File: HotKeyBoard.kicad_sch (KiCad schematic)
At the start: 414 parts, among them J1 Conn_01x04_Pin, J2 Conn_01x04_Pin, J3 USB_VOLTAGE Measuring Point, J4 LED_VOLTAGE Measuring Point 1, J5 LED_VOLTAGE Measuring Point 2, Q1 IRLZ34N, Q2 IRLZ34N, Q3 IRLZ34N, Q4 IRLZ34N, Q5 IRLZ34N, Q6 IRLZ34N, SW1 SW_Push, SW10 SW_Push, SW11 SW_Push, SW12 SW_Push, SW13 SW_Push, SW14 SW_Push, SW15 SW_Push, SW16 SW_Push, SW17 SW_Push, SW18 SW_Push, SW19 SW_Push, SW2 SW_Push, SW20 SW_Push, SW21 SW_Push, SW22 SW_Push, SW23 SW_Push, SW24 SW_Push, SW25 SW_Push, SW26 SW_Push, SW27 SW_Push, SW28 SW_Push, SW29 SW_Push, SW3 SW_Push, SW30 SW_Push, SW31 SW_Push, SW32 SW_Push, SW33 SW_Push, SW34 SW_Push, SW35 SW_Push, SW36 SW_Push, SW37 SW_Push, SW38 SW_Push, SW39 SW_Push, SW4 SW_Push, SW40 SW_Push, SW41 SW_Push, SW42 SW_Push, SW43 SW_Push, SW44 SW_Push, SW45 SW_Push, SW46 SW_Push, SW47 SW_Push, SW48 SW_Push, SW49 SW_Push, SW5 SW_Push, SW50 SW_Push, SW51 SW_Push, SW52 SW_Push, SW53 SW_Push, SW54 SW_Push, SW55 SW_Push, SW56 SW_Push, SW57 SW_Push, SW58 SW_Push, SW59 SW_Push, SW6 SW_Push, SW60 SW_Push, SW61 SW_Push, SW62 SW_Push, SW63 SW_Push, SW64 SW_Push, SW65 SW_Push, SW66 SW_Push, SW67 SW_Push, SW68 SW_Push, SW69 SW_Push, SW7 SW_Push, SW70 SW_Push, SW71 SW_Push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

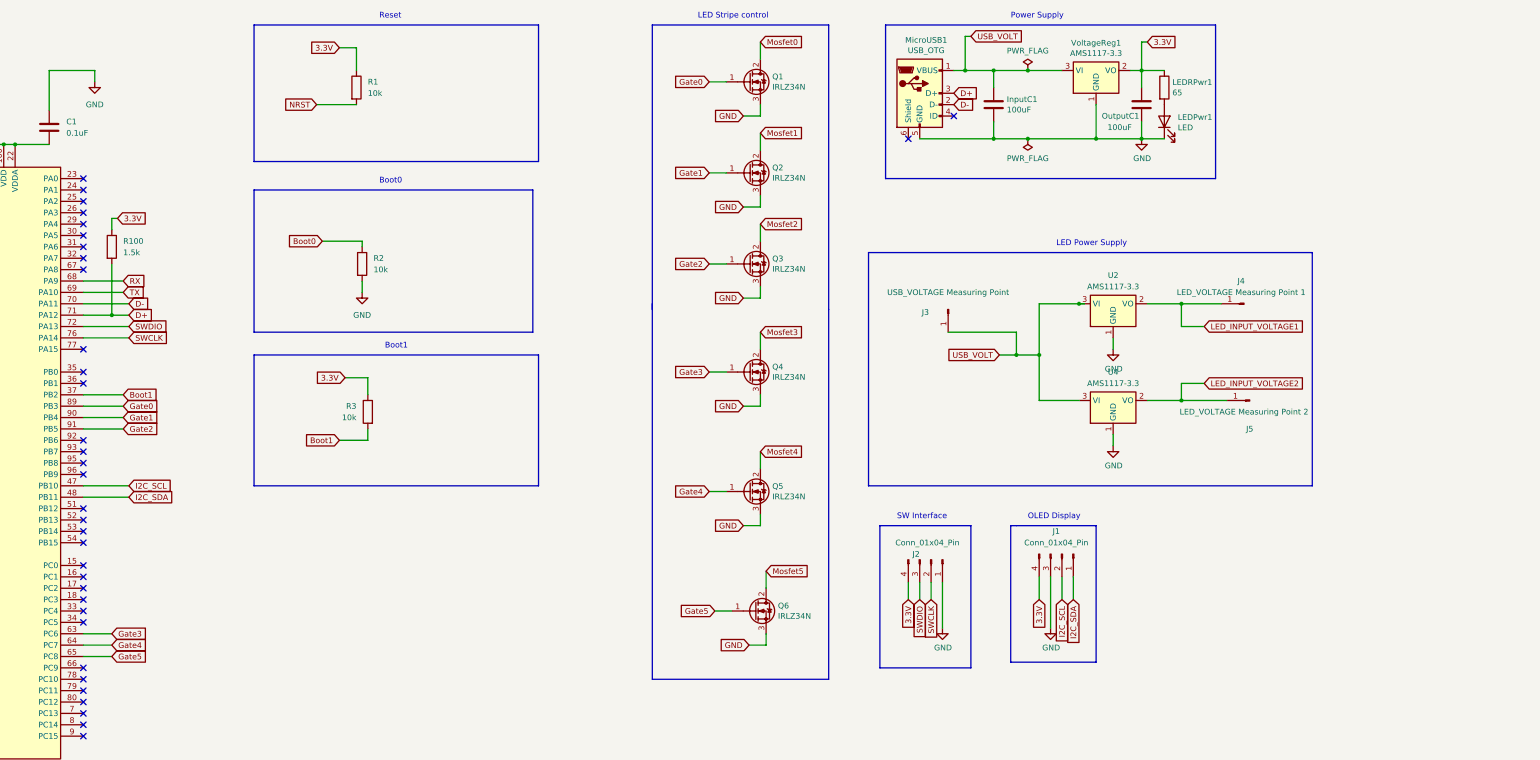
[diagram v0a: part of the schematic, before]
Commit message: Added overbridging of mosfets
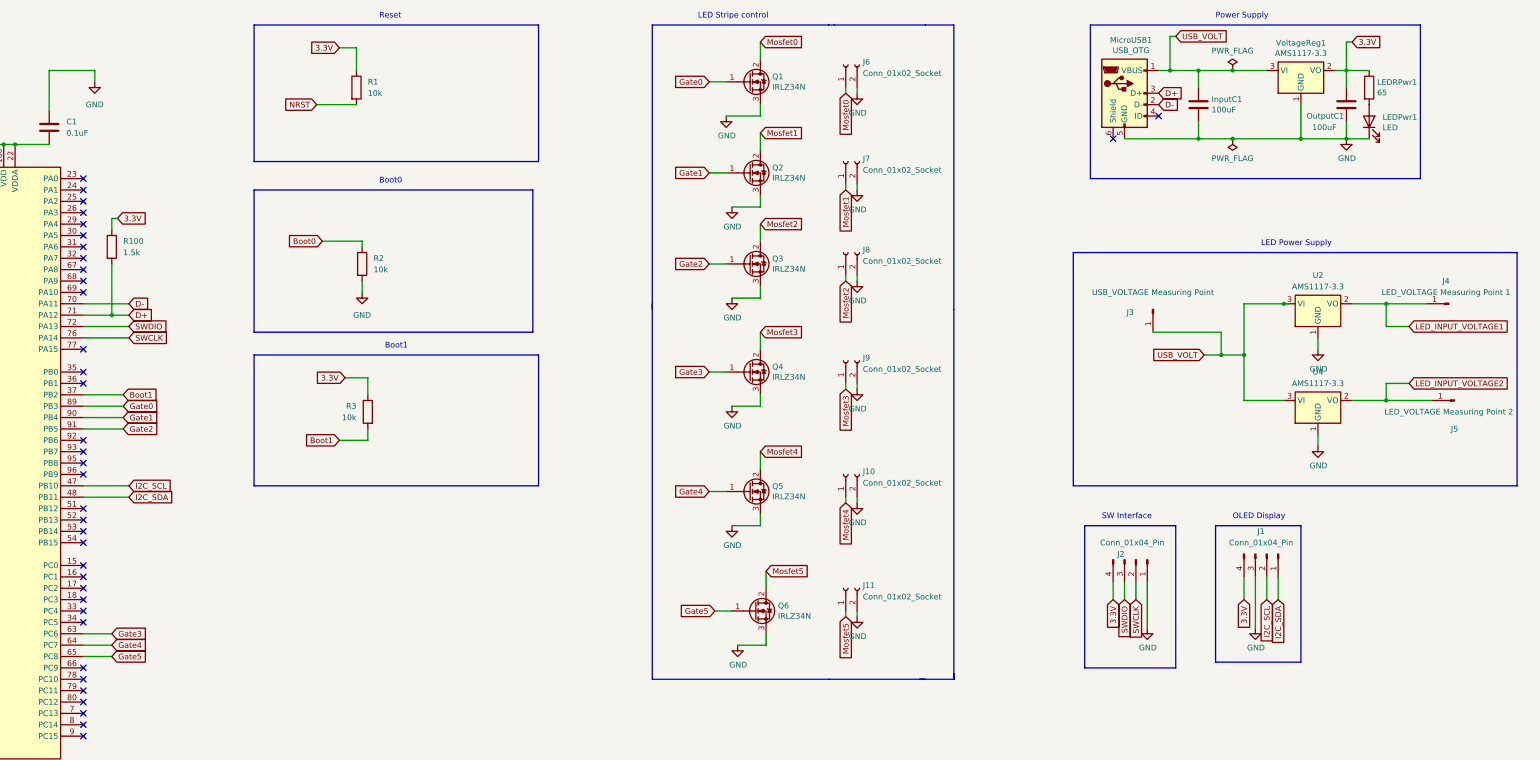
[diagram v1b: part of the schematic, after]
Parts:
- added J10, J11, J6, J7, J8, J9: Conn_01x02_Socket, Connector_PinHeader_2.54mm:PinHeader_1x02_P2.54mm_Vertical, symbol Connector:Conn_01x02_Socket
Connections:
- net GND: now also J10.2 (Pin_2), J11.2 (Pin_2), J6.2 (Pin_2), J7.2 (Pin_2), J8.2 (Pin_2), J9.2 (Pin_2)
- net Mosfet0: now also J6.1 (Pin_1)
- net Mosfet1: now also J7.1 (Pin_1)
- net Mosfet2: now also J8.1 (Pin_1)
- net Mosfet3: now also J9.1 (Pin_1)
- net Mosfet4: now also J10.1 (Pin_1)
- net Mosfet5: now also J11.1 (Pin_1)
- net RX: no longer names the net of U1.68 (PA9)
- net TX: no longer names the net of U1.69 (PA10)
- no-connect marks 37 -> 39
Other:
- moved on the sheet: InputC1, J1, J2, J3, J4, J5, LEDPwr1, LEDRPwr1, MicroUSB1, OutputC1, U2, U4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

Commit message: Added THT micro usb
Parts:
- MicroUSB1: footprint Connector_USB:USB_Micro-B_Molex_47346-0001 -> Connector_USB:USB_Micro-B_Amphenol_10118194_Horizontal; LCSC (none) -> C114094
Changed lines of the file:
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@@
       (effects (font (size 1.27 1.27)))
     )
-    (property "Footprint" "Connector_USB:USB_Micro-B_Molex_47346-0001" (at 499.11 36.83 0)
+    (property "Footprint" "Connector_USB:USB_Micro-B_Amphenol_10118194_Horizontal" (at 499.11 36.83 0)
       (effects (font (size 1.27 1.27)) hide)
     )
@@
       (effects (font (size 1.27 1.27)) hide)
     )
+    (property "LCSC" "C114094" (at 495.3 35.56 0)
+      (effects (font (size 1.27 1.27)) hide)
+    )

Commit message: Changed micro usb port
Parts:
- MicroUSB1: footprint Connector_USB:USB_Micro-B_Amphenol_10118194_Horizontal -> Library:MICRO-USB_SMD_USB-MR-D-034; LCSC C114094 -> C2927005
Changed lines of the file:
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@@
       (effects (font (size 1.27 1.27)))
     )
-    (property "Footprint" "Connector_USB:USB_Micro-B_Amphenol_10118194_Horizontal" (at 499.11 36.83 0)
+    (property "Footprint" "Library:MICRO-USB_SMD_USB-MR-D-034" (at 499.11 36.83 0)
       (effects (font (size 1.27 1.27)) hide)
     )
@@
       (effects (font (size 1.27 1.27)) hide)
     )
-    (property "LCSC" "C114094" (at 495.3 35.56 0)
+    (property "LCSC" "C2927005" (at 495.3 35.56 0)
       (effects (font (size 1.27 1.27)) hide)
     )

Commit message: Switched micro usb again
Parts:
- MicroUSB1: footprint Library:MICRO-USB_SMD_USB-MR-D-034 -> Library:MICRO-USB-SMD_5P-P0.65-H-F_U254-051T-4BH81-S2S; LCSC C2927005 -> C381144
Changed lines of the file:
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@@
       (effects (font (size 1.27 1.27)))
     )
-    (property "Footprint" "Library:MICRO-USB_SMD_USB-MR-D-034" (at 499.11 36.83 0)
+    (property "Footprint" "Library:MICRO-USB-SMD_5P-P0.65-H-F_U254-051T-4BH81-S2S" (at 499.11 36.83 0)
       (effects (font (size 1.27 1.27)) hide)
     )
@@
       (effects (font (size 1.27 1.27)) hide)
     )
-    (property "LCSC" "C2927005" (at 495.3 35.56 0)
+    (property "LCSC" "C381144" (at 495.3 35.56 0)
       (effects (font (size 1.27 1.27)) hide)
     )

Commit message: Finished schematic
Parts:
- removed C1: 0.1uF, Capacitor_SMD:C_0402_1005Metric, symbol Device:C
- removed C2: 1uF, Capacitor_SMD:C_0603_1608Metric, symbol Device:C
- removed InputC1, OutputC1: 100uF, Capacitor_SMD:C_1206_3216Metric, symbol Device:C
- removed J10, J11, J7, J8, J9: Conn_01x02_Socket, Connector_PinHeader_2.54mm:PinHeader_1x02_P2.54mm_Vertical, symbol Connector:Conn_01x02_Socket
- removed J2: Conn_01x04_Pin, Connector_PinHeader_2.54mm:PinHeader_1x04_P2.54mm_Vertical, symbol Connector:Conn_01x04_Pin
- removed J3: USB_VOLTAGE Measuring Point, Connector_PinHeader_2.54mm:PinHeader_1x01_P2.54mm_Vertical, symbol Connector:Conn_01x01_Pin
- removed J4: LED_VOLTAGE Measuring Point 1, Connector_PinHeader_2.54mm:PinHeader_1x01_P2.54mm_Vertical, symbol Connector:Conn_01x01_Pin
- removed J5: LED_VOLTAGE Measuring Point 2, Connector_PinHeader_2.54mm:PinHeader_1x01_P2.54mm_Vertical, symbol Connector:Conn_01x01_Pin
- removed LEDPwr1: LED, LED_SMD:LED_0402_1005Metric, symbol Device:LED
- removed LEDRPwr1: 65, Resistor_SMD:R_0603_1608Metric, symbol Device:R
- removed MicroUSB1: USB_OTG, Library:MICRO-USB-SMD_5P-P0.65-H-F_U254-051T-4BH81-S2S, symbol Connector:USB_OTG
- removed Q2, Q3, Q4, Q5, Q6: IRLZ34N, Package_TO_SOT_SMD:TO-263-2, symbol Transistor_FET:IRLZ34N
- removed R1, R2, R3: 10k, Resistor_SMD:R_0603_1608Metric, symbol Device:R
- removed R100: 1.5k, Resistor_SMD:R_0603_1608Metric, symbol Device:R
- removed U1: STM32F103VBTx, Package_QFP:LQFP-100_14x14mm_P0.5mm, symbol MCU_ST_STM32F1:STM32F103VBTx
- removed U2, U4, VoltageReg1: AMS1117-3.3, Package_TO_SOT_SMD:SOT-223-3_TabPin2, symbol Regulator_Linear:AMS1117-3.3
- added J2, J3: Conn_01x20_Pin, Connector_PinHeader_2.54mm:PinHeader_1x20_P2.54mm_Vertical, symbol Connector:Conn_01x20_Pin
- R10, R11, R12, R13, R14, R15, R16, R17, R18, R19, R20, R21, R22, R23, R24, R25, R26, R27, R28, R29, R30, R31, R32, R33, R34, R35, R36, R37, R38, R39, R4, R40, R42, R43, R44, R45, R46, R47, R48, R49, R5, R50, R51, R52, R53, R54, R55, R56, R57, R58, R59, R6, R60, R61, R62, R63, R64, R65, R66, R67, R68, R69, R7, R70, R71, R72, R73, R74, R75, R76, R77, R78, R79, R8, R80, R81, R82, R83, R84, R85, R86, R87, R88, R89, R9, R90, R91, R92, R93, R94, R95, R96, R97, R98, R99: LCSC C307279 -> C881395
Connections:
- net LED_INPUT_VOLTAGE2 is gone; now on net 5V: R52.1, R53.1, R54.1, R55.1, R56.1, R57.1, R58.1, R59.1, R60.1, R61.1, R62.1, R63.1, R64.1, R65.1, R66.1, R67.1, R68.1, R69.1, R70.1, R71.1, R72.1, R73.1, R74.1, R75.1, R76.1, R77.1, R78.1, R79.1, R80.1, R81.1, R82.1, R83.1, R84.1, R85.1, R86.1, R87.1, R88.1, R89.1, R90.1, R91.1, R92.1, R93.1, R94.1, R95.1, R96.1, R97.1, R98.1, R99.1
- net Mosfet1 is gone; now on net Mosfet0: D113.1 (K), D114.1 (K), D115.1 (K), D116.1 (K), D117.1 (K), D118.1 (K), D119.1 (K), D120.1 (K), D121.1 (K), D122.1 (K), D123.1 (K), D124.1 (K), D125.1 (K), D126.1 (K), D127.1 (K), D128.1 (K)
- net Mosfet2 is gone; now on net Mosfet0: D129.1 (K), D130.1 (K), D131.1 (K), D132.1 (K), D133.1 (K), D134.1 (K), D135.1 (K), D136.1 (K), D137.1 (K), D138.1 (K), D139.1 (K), D140.1 (K), D141.1 (K), D142.1 (K), D143.1 (K), D144.1 (K)
- net Mosfet3 is gone; now on net Mosfet0: D145.1 (K), D146.1 (K), D147.1 (K), D148.1 (K), D149.1 (K), D150.1 (K), D151.1 (K), D152.1 (K), D153.1 (K), D154.1 (K), D155.1 (K), D156.1 (K), D157.1 (K), D158.1 (K), D159.1 (K), D160.1 (K)
- net Mosfet4 is gone; now on net Mosfet0: D161.1 (K), D162.1 (K), D163.1 (K), D164.1 (K), D165.1 (K), D166.1 (K), D167.1 (K), D168.1 (K), D169.1 (K), D170.1 (K), D171.1 (K), D172.1 (K), D173.1 (K), D174.1 (K), D175.1 (K), D176.1 (K)
- net Mosfet5 is gone; now on net Mosfet0: D177.1 (K), D178.1 (K), D179.1 (K), D180.1 (K), D181.1 (K), D182.1 (K), D183.1 (K), D184.1 (K), D185.1 (K), D186.1 (K), D187.1 (K), D188.1 (K), D189.1 (K), D190.1 (K), D191.1 (K), D192.1 (K)
- net 3.3V: now also J2.20 (Pin_20), J3.3 (Pin_3)
- net Col0: now also J3.8 (Pin_8)
- net Col1: now also J3.7 (Pin_7)
- net Col10: now also J2.1 (Pin_1)
- net Col11: now also J2.2 (Pin_2)
- net Col12: now also J2.3 (Pin_3)
- net Col13: now also J2.4 (Pin_4)
- net Col14: now also J2.5 (Pin_5)
- net Col2: now also J3.9 (Pin_9)
- net Col3: now also J2.13 (Pin_13)
- net Col4: now also J2.14 (Pin_14)
- net Col5: now also J2.15 (Pin_15)
- net Col6: now also J2.16 (Pin_16)
- net Col7: now also J2.17 (Pin_17)
- net Col8: now also J3.6 (Pin_6)
- net Col9: now also J3.5 (Pin_5)
- net GND: now also J2.19 (Pin_19), J3.1 (Pin_1), J3.2 (Pin_2)
- net Row0: now also J3.16 (Pin_16)
- net Row1: now also J3.15 (Pin_15)
- net Row2: now also J3.14 (Pin_14)
- net Row3: now also J3.13 (Pin_13)
- net Row4: now also J3.12 (Pin_12)
- net Row5: now also J3.11 (Pin_11)
- net Gate0 renamed LEDControl
- net LEDControl: now also J2.6 (Pin_6)
- net LED_INPUT_VOLTAGE1 renamed 5V
- net 5V: now also J2.18 (Pin_18)
- new net A10: J2.7 (Pin_7)
- new net A11: J2.8 (Pin_8)
- new net A12: J2.9 (Pin_9)
- new net A15: J2.10 (Pin_10)
- new net A6: J3.10 (Pin_10)
- new net B3: J2.11 (Pin_11)
- new net B4: J2.12 (Pin_12)
- new net C13: J3.19 (Pin_19)
- new net C14: J3.18 (Pin_18)
- new net C15: J3.17 (Pin_17)
- new net Reset: J3.4 (Pin_4)
- new net VB: J3.20 (Pin_20)
- no-connect marks 39 -> 0
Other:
- note removed: "Boot0"
- note removed: "Boot1"
- note removed: "LED Power Supply"
- note removed: "Power Supply"
- note removed: "Reset"
- note removed: "SW Interface"
- moved on the sheet: D1, D10, D100, D101, D102, D103, D104, D105, D106, D107, D108, D109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

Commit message: Finished layout
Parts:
- Q1: footprint Package_TO_SOT_SMD:TO-263-2 -> Package_TO_SOT_THT:TO-220-3_Vertical
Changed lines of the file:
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@@
       (effects (font (size 1.27 1.27)) (justify left))
     )
-    (property "Footprint" "Package_TO_SOT_SMD:TO-263-2" (at 411.48 224.155 0)
+    (property "Footprint" "Package_TO_SOT_THT:TO-220-3_Vertical" (at 411.48 224.155 0)
       (effects (font (size 1.27 1.27) italic) (justify left) hide)
     )

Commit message: Fixed resistor
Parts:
- R41: LCSC C307279 -> C881395
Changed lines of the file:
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@@
       (effects (font (size 1.27 1.27)) hide)
     )
-    (property "LCSC" "C307279" (at 139.7 246.38 0)
+    (property "LCSC" "C881395" (at 139.7 246.38 0)
       (effects (font (size 1.27 1.27)) hide)
     )

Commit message: Added multiple mosfets
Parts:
- added J4, J5: Conn_01x02_Socket, Connector_PinHeader_2.54mm:PinHeader_1x02_P2.54mm_Vertical, symbol Connector:Conn_01x02_Socket
- added Q2, Q3: IRLZ34N, Package_TO_SOT_THT:TO-220-3_Vertical, symbol Transistor_FET:IRLZ34N
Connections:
- net GND: now also J4.2 (Pin_2), J5.2 (Pin_2), Q2.3 (S), Q3.3 (S)
- net Mosfet0: no longer D113.1 (K), D114.1 (K), D115.1 (K), D116.1 (K), D117.1 (K), D118.1 (K), D119.1 (K), D120.1 (K), D121.1 (K), D122.1 (K), D123.1 (K), D124.1 (K), D125.1 (K), D126.1 (K), D127.1 (K), D128.1 (K), D129.1 (K), D130.1 (K), D131.1 (K), D132.1 (K), D133.1 (K), D134.1 (K), D135.1 (K), D136.1 (K), D137.1 (K), D138.1 (K), D139.1 (K), D140.1 (K), D141.1 (K), D142.1 (K), D143.1 (K), D144.1 (K), D145.1 (K), D146.1 (K), D147.1 (K), D148.1 (K), D149.1 (K), D150.1 (K), D151.1 (K), D152.1 (K), D153.1 (K), D154.1 (K), D155.1 (K), D156.1 (K), D157.1 (K), D158.1 (K), D159.1 (K), D160.1 (K), D161.1 (K), D162.1 (K), D163.1 (K), D164.1 (K), D165.1 (K), D166.1 (K), D167.1 (K), D168.1 (K), D169.1 (K), D170.1 (K), D171.1 (K), D172.1 (K), D173.1 (K), D174.1 (K), D175.1 (K), D176.1 (K), D177.1 (K), D178.1 (K), D179.1 (K), D180.1 (K), D181.1 (K), D182.1 (K), D183.1 (K), D184.1 (K), D185.1 (K), D186.1 (K), D187.1 (K), D188.1 (K), D189.1 (K), D190.1 (K), D191.1 (K), D192.1 (K)
- net A10 renamed LEDControl1
- net LEDControl1: now also Q2.1 (G)
- net A6 renamed LEDControl2
- net LEDControl2: now also Q3.1 (G)
- net LEDControl renamed LEDControl0
- new net Mosfet1: D113.1 (K), D114.1 (K), D115.1 (K), D116.1 (K), D117.1 (K), D118.1 (K), D119.1 (K), D120.1 (K), D121.1 (K), D122.1 (K), D123.1 (K), D124.1 (K), D125.1 (K), D126.1 (K), D127.1 (K), D128.1 (K), D129.1 (K), D130.1 (K), D131.1 (K), D132.1 (K), D133.1 (K), D134.1 (K), D135.1 (K), D136.1 (K), D137.1 (K), D138.1 (K), D139.1 (K), D140.1 (K), D141.1 (K), D142.1 (K), D143.1 (K), D144.1 (K), D145.1 (K), D146.1 (K), D147.1 (K), D148.1 (K), D149.1 (K), D150.1 (K), D151.1 (K), D152.1 (K), D153.1 (K), D154.1 (K), D155.1 (K), D156.1 (K), D157.1 (K), D158.1 (K), D159.1 (K), D160.1 (K), D161.1 (K), D162.1 (K), D163.1 (K), D164.1 (K), D165.1 (K), D166.1 (K), D167.1 (K), D168.1 (K), D169.1 (K), D170.1 (K), D171.1 (K), D172.1 (K), D173.1 (K), D174.1 (K), D175.1 (K), D176.1 (K), J4.1 (Pin_1), Q2.2 (D)
- new net Mosfet2: D177.1 (K), D178.1 (K), D179.1 (K), D180.1 (K), D181.1 (K), D182.1 (K), D183.1 (K), D184.1 (K), D185.1 (K), D186.1 (K), D187.1 (K), D188.1 (K), D189.1 (K), D190.1 (K), D191.1 (K), D192.1 (K), J5.1 (Pin_1), Q3.2 (D)
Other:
- moved on the sheet: J6, Q1
